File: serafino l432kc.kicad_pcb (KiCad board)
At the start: 4 copper layers, 17.8 x 35.6 mm, 31 parts, among them J1 USB_B_Micro, J2 Conn_01x14, J3 Conn_01x14, Q1 SI3401A-TP, SW1 SW_Push, SW2 SW_Push, U1 AP2112K-3.3, U2 USBLC6-2SC6, U3 STM32L432KCUx, Y1 32.768K

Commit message: Avances
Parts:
- added G***: LOGO, serafino l432kc:big_cupid, B.Cu at (197.5, 98.0)
- added G***: LOGO, serafino l432kc:cupid, F.Cu at (197.4, 104.9)
- added G***: LOGO, serafino l432kc:logo_materiam, F.Cu at (191.7, 109.8)
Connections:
- J2 pad 13: BOOT0 -> PA8
- J2 pad 2: EN -> VHIGH
- J2 pad 3: VHIGH -> CAN_TD
- J3 pad 4: PA8 -> CAN_RD
- U2 pad 4: USB_D+ -> CAN_TD
- U2 pad 6: USB_D- -> CAN_RD
- U3 pad 21: USB_D- -> CAN_RD
- U3 pad 22: USB_D+ -> CAN_TD
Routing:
- net CAN_TD: track 0.00 -> 27.4 mm, vias 0 -> 1
- net PA8: track 10.9 -> 33.0 mm, vias 0 -> 1
- net CAN_RD: track 0.00 -> 12.1 mm
- net USB_D-: track 7.98 -> 0.00 mm
- net USB_D+: track 7.15 -> 0.00 mm
- net EN: track 15.6 -> 11.1 mm
- net BOOT0: track 17.9 -> 14.5 mm
- net VHIGH: track 18.5 -> 21.1 mm
- net I2C1_SCL: vias 0 -> 1
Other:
- board text added: "CANRD"
- board text added: "CANTD"
- board text added: "VH"
- board text removed: "EN"
- board text removed: "PA8"
- board text removed: "VHIGH"

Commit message: Silk screen
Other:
- board text added: "* STM32L432KC ARM Cortex M4 * 64KB SRAM/256KB Flash/80Mhz * Max Supply Voltage Vin: 6.0v * Power Supply Max Iout: 600ma * Press RESET while holding BOOT0 to enter DFU mode."
- board text added: "<-BOOT0 / SWO"
- board text removed: "* STM32L432KC ARM Cortex M4 * 64KB SRAM/256KB Flash/80Mhz * Embedded USB DFU Bootloader Press RESET while holding BOOT0 to enter DFU mode."
- board text removed: "<-SW0"

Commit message: Finished back labels
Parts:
- removed the G*** at (197.5, 98.0)
- moved G*** 0.43 mm to (191.7, 109.4)
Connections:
- net EN renamed Net-(R5-Pad2)
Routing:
- net Net-(R5-Pad2): track 11.1 -> 2.42 mm, vias 1 -> 0
- net CAN_TD: track 27.4 -> 22.4 mm
- net PA8: track 33.0 -> 30.6 mm
- net GND: track 42.2 -> 43.7 mm
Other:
- board text added: "* STM32L432KC ARM Cortex M4 * 64KB SRAM/256KB Flash/80Mhz * Max Supply Voltage Vin: 6.0v * Power Supply Max Iout: 600ma * Source/Sink per pin <= 20ma * Source/Sink all pins <= 100ma Press RESET while holding BOOT0 to enter DFU mode."
- board text removed: "* STM32L432KC ARM Cortex M4 * 64KB SRAM/256KB Flash/80Mhz * Max Supply Voltage Vin: 6.0v * Power Supply Max Iout: 600ma * Press RESET while holding BOOT0 to enter DFU mode."

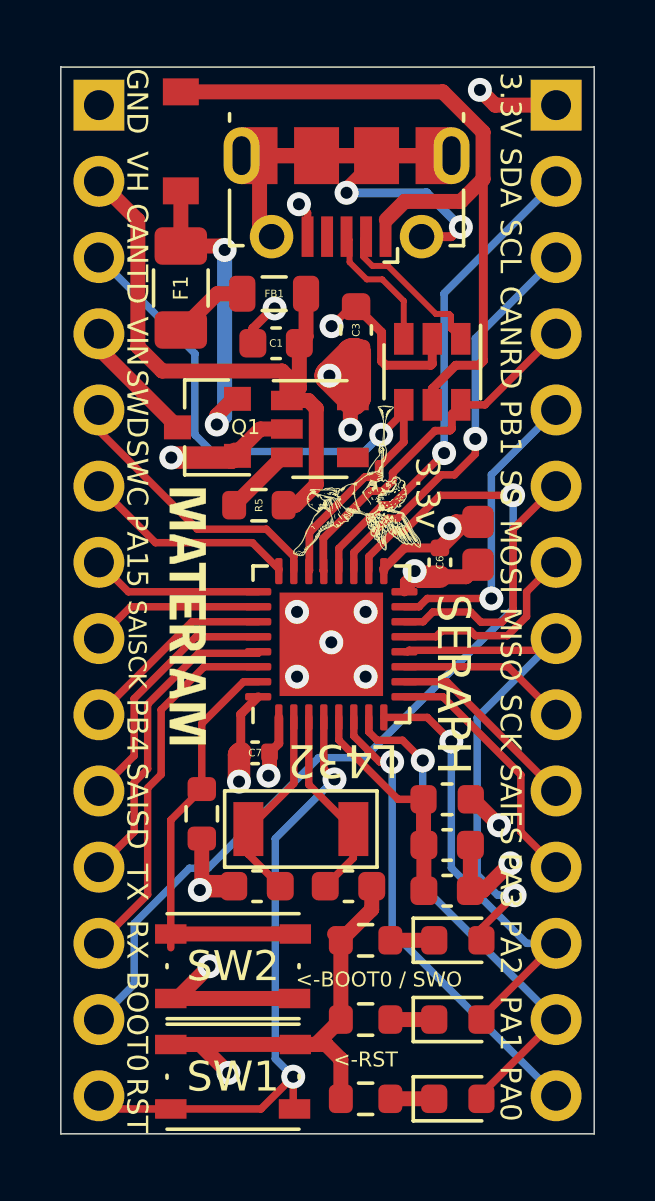
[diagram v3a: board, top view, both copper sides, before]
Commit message: Adjusted LED resistor values, changed BOOT0 to PA0 in silk screen.
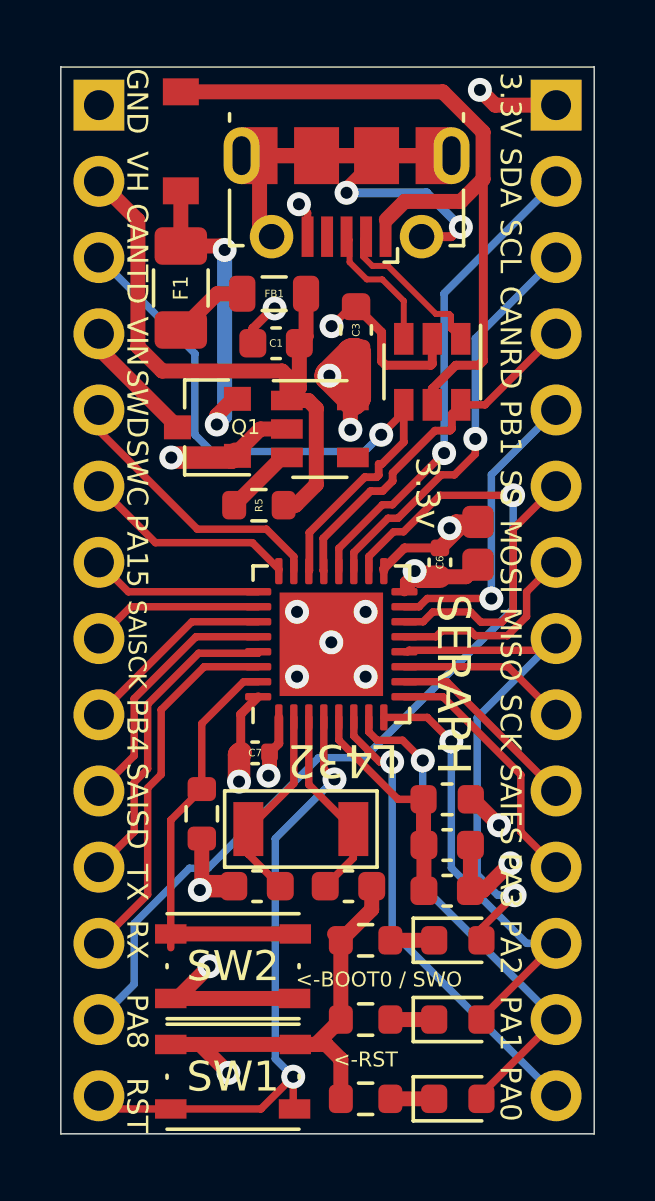
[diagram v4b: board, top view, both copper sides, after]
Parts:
- removed G***: LOGO, serafino l432kc:logo_materiam
- removed G***: LOGO, serafino l432kc:cupid
- R1: value 1K -> 270
- R4: value 1K -> 330
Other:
- board text added: "PA8"
- board text added: "v1.0"
- board text removed: "BOOT0"

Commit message: Disconnected LED2 from MISO since PA2 (LED1) is already on in DFU mode
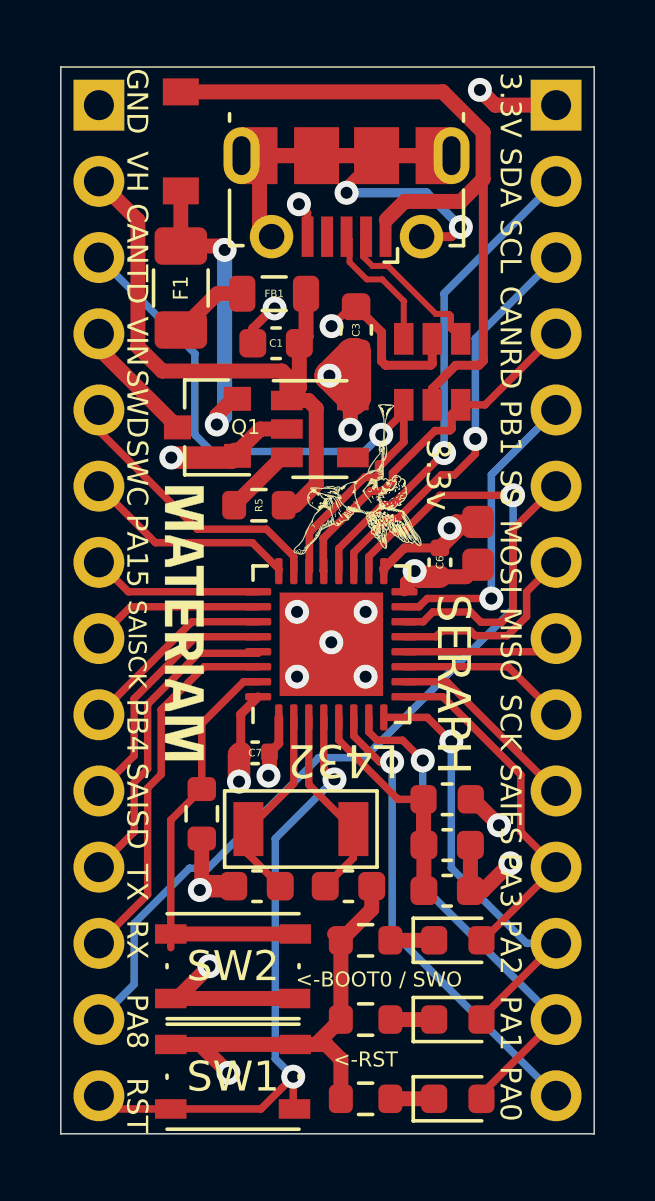
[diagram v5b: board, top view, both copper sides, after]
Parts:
- added G***: LOGO, serafino l432kc:big_cupid, B.Cu at (197.9, 97.9)
- added G***: LOGO, serafino l432kc:cupid, F.Cu at (197.4, 104.8)
- added G***: LOGO, serafino l432kc:logo_materiam, F.Cu at (191.6, 109.6)
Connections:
- D4 pad 2: SPI1_MISO -> LED2
- J3 pad 11: PA3 -> LED2
- U3 pad 9: PA3 -> LED2
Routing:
- net SPI1_MISO: track 17.7 -> 5.24 mm, vias 1 -> 0
- net LED2: track 0.00 -> 12.0 mm
- net PA3: track 8.52 -> 0.00 mm

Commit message: Seraph L4 v1.0
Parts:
- removed G***: LOGO, serafino l432kc:big_cupid
- removed G***: LOGO, serafino l432kc:cupid
- removed G***: LOGO, serafino l432kc:logo_materiam
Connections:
- net LED0 renamed PA1
- net LED1 renamed PA2
- net LED2 renamed PA3
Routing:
- net CAN_TD: track 22.4 -> 23.8 mm
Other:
- board text added: "* STM32L432KC Ultra Low Power * ARM Cortex M4 @ 80Mhz * 64KB SRAM/256KB Flash * Max Supply VIN: 6.0v/Iout: 600ma * Source/Sink per pin <= 20ma all pins <= 100ma Press RESET while holding BOOT0 to enter DFU programming mode."
- board text added: "<BOOT0/SWO"
- board text added: "<RST"
- board text added: "L4"
- board text added: "S S"
- board text added: "SAICK"
- board text removed: "* STM32L432KC ARM Cortex M4 * 64KB SRAM/256KB Flash/80Mhz * Max Supply Voltage Vin: 6.0v * Power Supply Max Iout: 600ma * Source/Sink per pin <= 20ma * Source/Sink all pins <= 100ma Press RESET while holding BOOT0 to enter DFU mode."
- board text removed: "<-BOOT0 / SWO"
- board text removed: "<-RST"
- board text removed: "L432"
- board text removed: "SAISCK"
- board text removed: "SS"

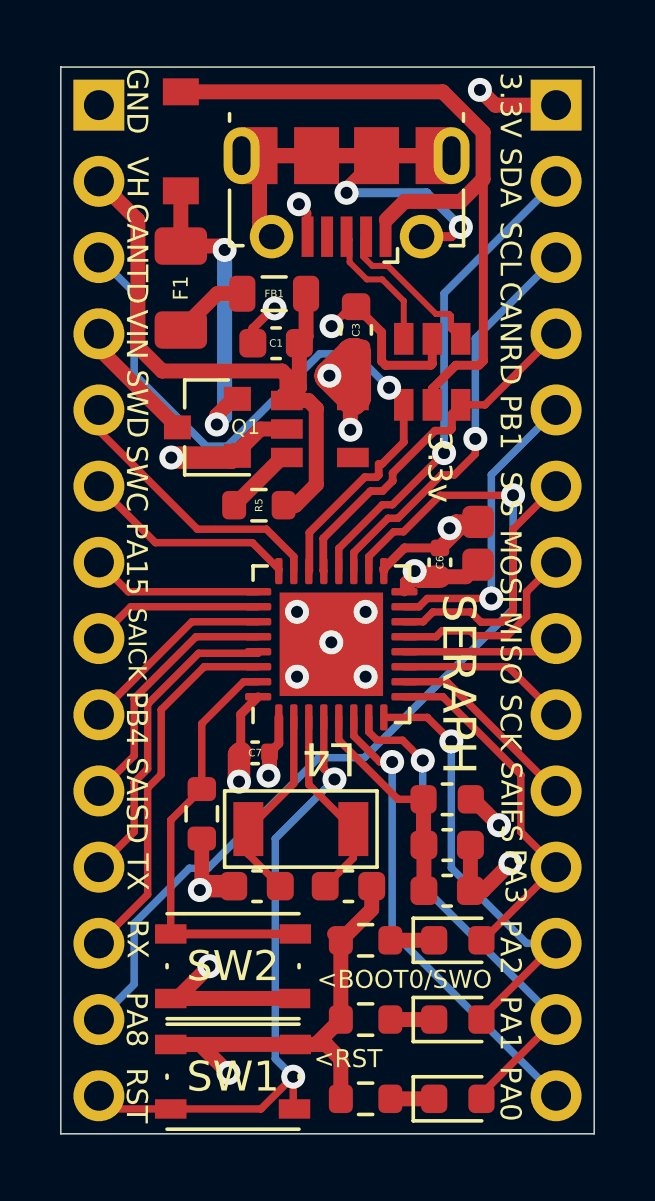
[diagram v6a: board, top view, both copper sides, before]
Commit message: USB placement correction
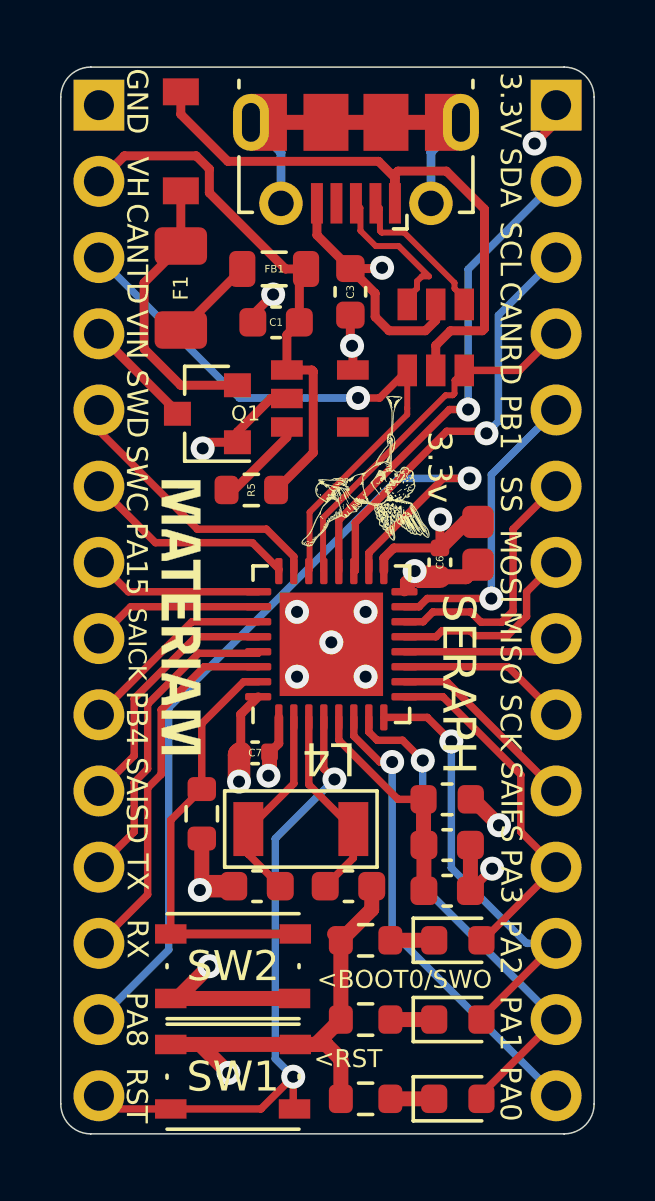
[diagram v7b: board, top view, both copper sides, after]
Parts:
- added G***: LOGO, serafino l432kc:logo_materiam, F.Cu at (191.5, 109.4)
- added G***: LOGO, serafino l432kc:cupid, F.Cu at (197.7, 104.5)
- moved C3 1.28 mm to (197.1, 98.6)
- moved U2 1.15 mm to (199.9, 100.1)
- moved J1 1.15 mm to (197.3, 94.1)
- moved U1 1.02 mm to (196.1, 102.1)
- moved FB1 0.83 mm to (194.6, 97.8)
- moved C1 0.70 mm to (194.6, 99.6)
- moved R5 0.57 mm to (193.8, 105.2)
- moved Q1 0.45 mm to (192.3, 102.6)
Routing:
- net Net-(J1-Pad6): track 22.4 -> 13.2 mm, vias 2 -> 0
- net +3V3: track 22.5 -> 17.7 mm, vias 7 -> 6
- net +5V: track 25.1 -> 20.8 mm
- net CAN_TD: track 23.8 -> 20.6 mm
- net VHIGH: track 21.1 -> 18.3 mm
- net Net-(D2-Pad1): track 10.5 -> 9.39 mm, vias 2 -> 0
- net PA8: track 30.6 -> 29.5 mm
- net USB_CONN_D+: track 4.50 -> 5.26 mm
- net Net-(R5-Pad2): track 2.42 -> 3.08 mm
- net GND: track 43.7 -> 44.1 mm, vias 14 -> 13
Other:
- outline, holes or cut-outs redrawn
- board text added: "SS"
- board text removed: "S S"

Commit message: ajustes
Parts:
- added G***: LOGO, serafino l432kc:big_cupid, B.Cu at (197.8, 98.9)
